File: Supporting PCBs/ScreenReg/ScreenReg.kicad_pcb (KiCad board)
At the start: 2 copper layers, 15.5 x 7 mm, 13 parts, among them U1 LM1117-1.8, U2 TPS7A21, U3 LM1117-3.3, U4 MIC23050-GYML

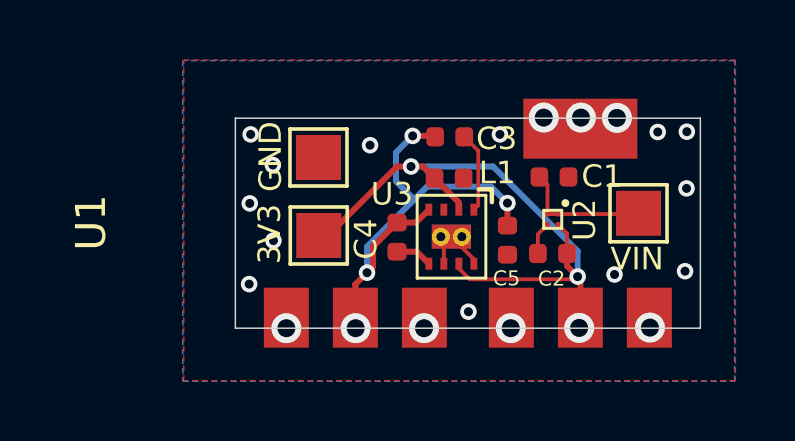
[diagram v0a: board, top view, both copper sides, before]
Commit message: + Motherboard is now V1.0 + Redesigned ScreenReg for improved reliability + Added both versions of ChargeBoost + Remove now redundant files/directories
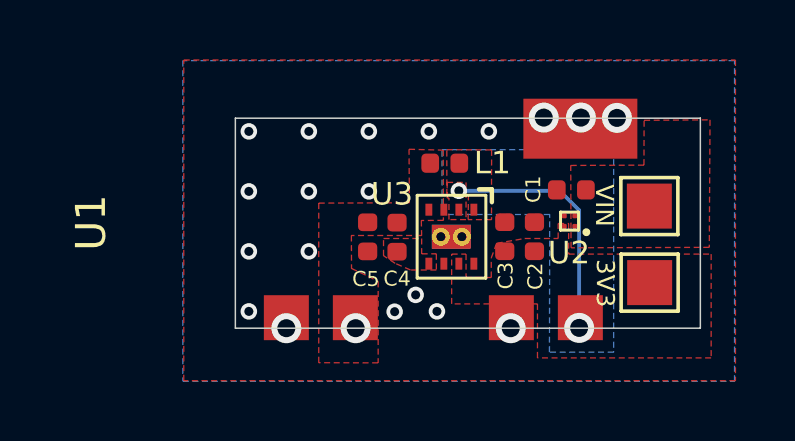
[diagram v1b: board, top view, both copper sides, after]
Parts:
- removed TP2: TestPoint, TestPoint:TestPoint_Pad_1.5x1.5mm
- moved TP3 11.1 mm to (13.8, -1.52)
- moved C5 4.66 mm to (4.41, -3.04)
- moved C3 2.69 mm to (8.98, -3.05), turned to 90 degrees
- moved L1 0.90 mm to (6.98, -5.50)
- moved C2 0.82 mm to (9.97, -3.05), turned to 90 degrees
- moved C1 0.72 mm to (11.2, -4.61), turned to 180 degrees
- moved U2 0.56 mm to (11.1, -3.57), turned to 180 degrees
- moved TP1 0.43 mm to (13.8, -4.07)
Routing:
- net /1V8: track 15.7 -> 0.00 mm, vias 4 -> 1
- net /3V3: track 21.7 -> 7.92 mm, vias 3 -> 2
- net /VIN: track 4.39 -> 0.00 mm
- net /GND: track 3.25 -> 0.00 mm, vias 15 -> 16
- net Net-(L1-Pad1): track 2.68 -> 0.00 mm
- net Net-(C4-Pad2): track 1.23 -> 0.00 mm
- net Net-(U3-Pad3): vias 1 -> 0
- net Net-(U1-Pad3): vias 1 -> 0
- added copper zone on F.Cu, net /1V8
- added copper zone on B.Cu, net /3V3
- added copper zone on F.Cu, net /3V3
- added copper zone on F.Cu, net /VIN
- added copper zone on F.Cu, net Net-(C4-Pad2)
- added copper zone on F.Cu, net Net-(L1-Pad1)
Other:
- board text removed: "GND"
